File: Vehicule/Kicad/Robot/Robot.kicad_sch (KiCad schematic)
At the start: 3 parts, among them U1 ESP32-C3_SUPERMINI, U2 L293D, U3 Regulator-DFR0569

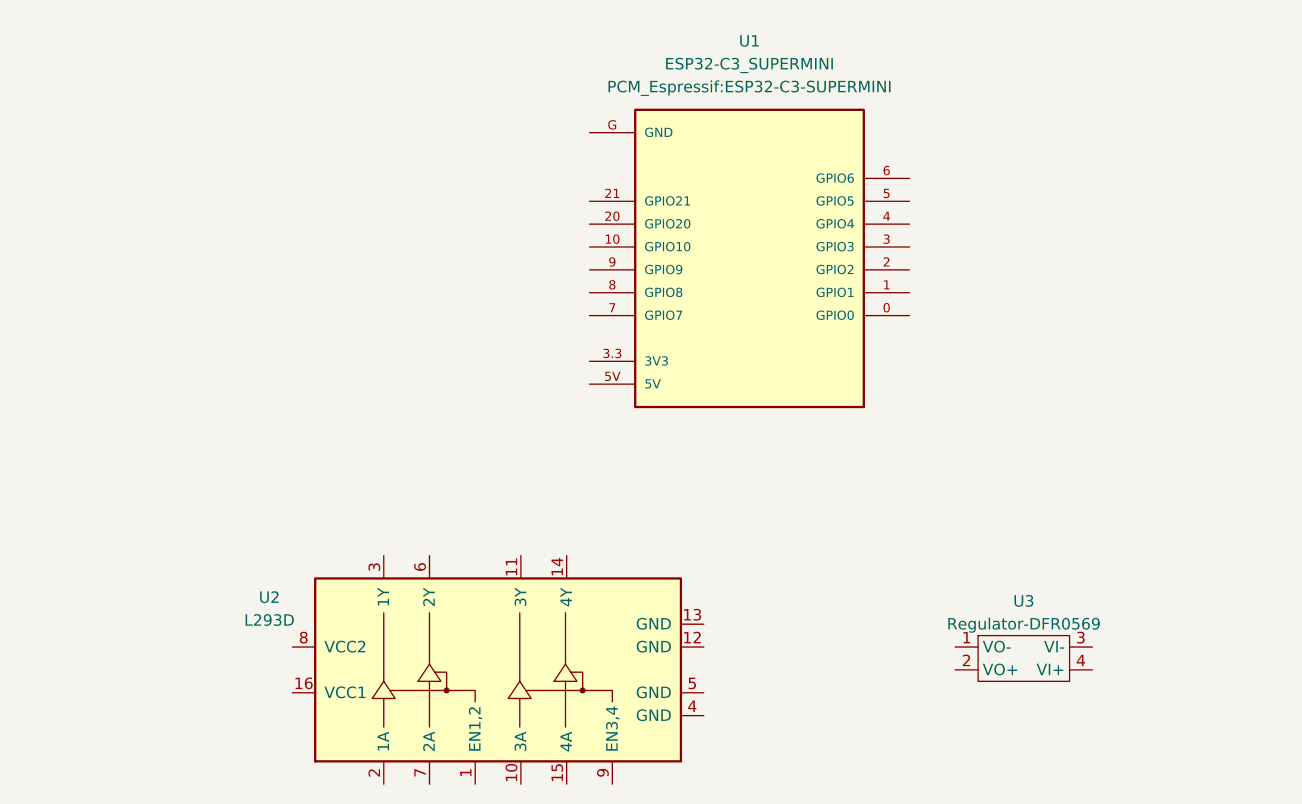
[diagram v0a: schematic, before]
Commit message: Schema et implantation du circuit pour le robot
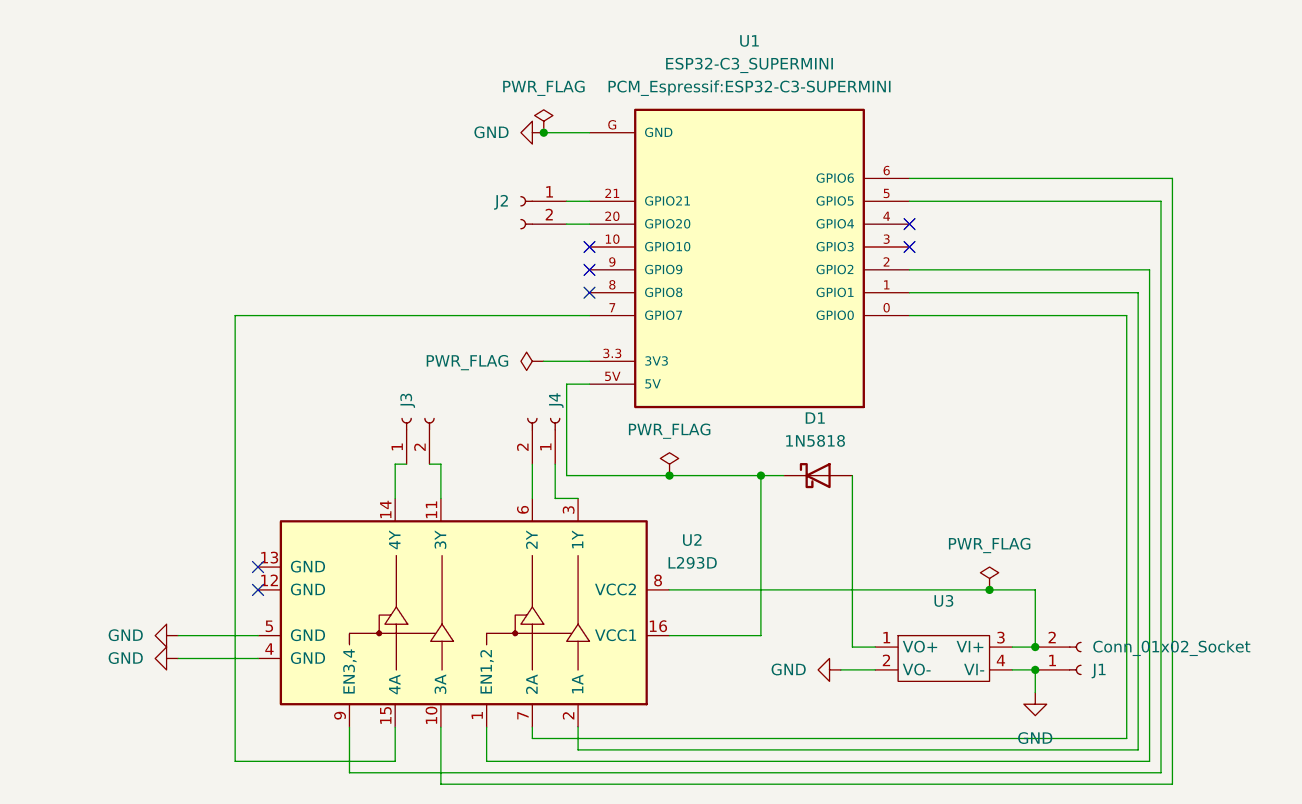
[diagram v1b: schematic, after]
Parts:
- added D1: 1N5818, Diode_THT:D_DO-41_SOD81_P10.16mm_Horizontal, symbol Diode:1N5818
- added J1, J2, J3, J4: Conn_01x02_Socket, Empreintes:CONN-2-PINS, symbol Connector:Conn_01x02_Socket
- U3: value Regulator-DFR0569 -> ~
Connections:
- net at U2.1 (EN1,2): now also U1.2 (GPIO2)
- net at U2.10 (3A): now also U1.6 (GPIO6)
- net at U2.11 (3Y): now also J3.2 (Pin_2)
- net at U2.14 (4Y): now also J3.1 (Pin_1)
- net at U2.15 (4A): now also U1.7 (GPIO7)
- net at U2.16 (VCC1): now also U1.5V, D1.1 (K)
- net at U2.2 (1A): now also U1.1 (GPIO1)
- net at U2.3 (1Y): now also J4.1 (Pin_1)
- net GND: now reaches U2.4 (GND)
- net GND: now also U1.G (GND), U2.5 (GND), U3.2 (VO-), U3.4 (VI-), J1.1 (Pin_1)
- net at U2.6 (2Y): now also J4.2 (Pin_2)
- net at U2.7 (2A): now also U1.0 (GPIO0)
- net at U2.8 (VCC2): now also U3.3 (VI+), J1.2 (Pin_2)
- net at U2.9 (EN3,4): now also U1.5 (GPIO5)
- net at U1.20 (GPIO20): now also J2.2 (Pin_2)
- net at U1.21 (GPIO21): now also J2.1 (Pin_1)
- net at U3.1 (VO+): now also D1.2 (A)
- no-connect marks 0 -> 7
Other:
- moved on the sheet: U2

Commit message: Transfert du SUPERMINI (composant et empreintes) dans les librairies locales (Anumby et Empreintes) Renommer Empreintes -> Anumby
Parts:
- J1, J2, J3, J4: footprint Empreintes:CONN-2-PINS -> Anumby:CONN-2-PINS
- U1: footprint PCM_Espressif:ESP32-C3-SUPERMINI -> Anumby:ESP32-C3-SUPERMINI
- U3: footprint Empreintes:Regulator-DFR0569 -> Anumby:Regulator-DFR0569
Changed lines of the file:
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@@
 			)
 		)
-		(property "Footprint" "Empreintes:CONN-2-PINS"
+		(property "Footprint" "Anumby:CONN-2-PINS"
 			(at 80.01 86.36 0)
 			(effects
@@
 			)
 		)
-		(property "Footprint" "PCM_Espressif:ESP32-C3-SUPERMINI"
+		(property "Footprint" "Anumby:ESP32-C3-SUPERMINI"
 			(at 101.6 49.53 0)
 			(effects
@@
 			)
 		)
-		(property "Footprint" "Empreintes:CONN-2-PINS"
+		(property "Footprint" "Anumby:CONN-2-PINS"
 			(at 63.5 86.36 0)
 			(effects
@@
 			)
 		)
-		(property "Footprint" "Empreintes:CONN-2-PINS"
+		(property "Footprint" "Anumby:CONN-2-PINS"
 			(at 138.43 114.3 0)
 			(effects
@@
 			)
 		)
-		(property "Footprint" "Empreintes:CONN-2-PINS"
+		(property "Footprint" "Anumby:CONN-2-PINS"
 			(at 76.2 62.23 0)
 			(effects
@@
 			)
 		)
-		(property "Footprint" "Empreintes:Regulator-DFR0569"
+		(property "Footprint" "Anumby:Regulator-DFR0569"
 			(at 121.92 111.76 0)
 			(effects

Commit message: Ajout de la couche de masse pour Robot Ajout d'un connecteur 1 pin Mise à jour de tous les PCB et les Schémas
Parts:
- removed J1, J2, J3, J4: Conn_01x02_Socket, Anumby:CONN-2-PINS, symbol Connector:Conn_01x02_Socket
- added J1, J2: Conn_01x02_Socket, Anumby:CONN-2-PINS, symbol Anumby:Conn_01x02_Socket
- added J3, J4, J5, J6: Conn_01x01_Socket, Anumby:CONN-1-PINS, symbol Anumby:Conn_01x01_Socket
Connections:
- net GND: now also J1.2 (Pin_2)
- net at U2.3 (1Y): now also J6.1 (Pin_1)
- net at U2.6 (2Y): now also J5.1 (Pin_1)
- net at U2.11 (3Y): now also J4.1 (Pin_1)
- net at U2.14 (4Y): now also J3.1 (Pin_1)
- net at U2.8 (VCC2), U3.3 (VI+): now also J1.1 (Pin_1)
- net at U1.20 (GPIO20): now also J2.2 (Pin_2)
- net at U1.21 (GPIO21): now also J2.1 (Pin_1)

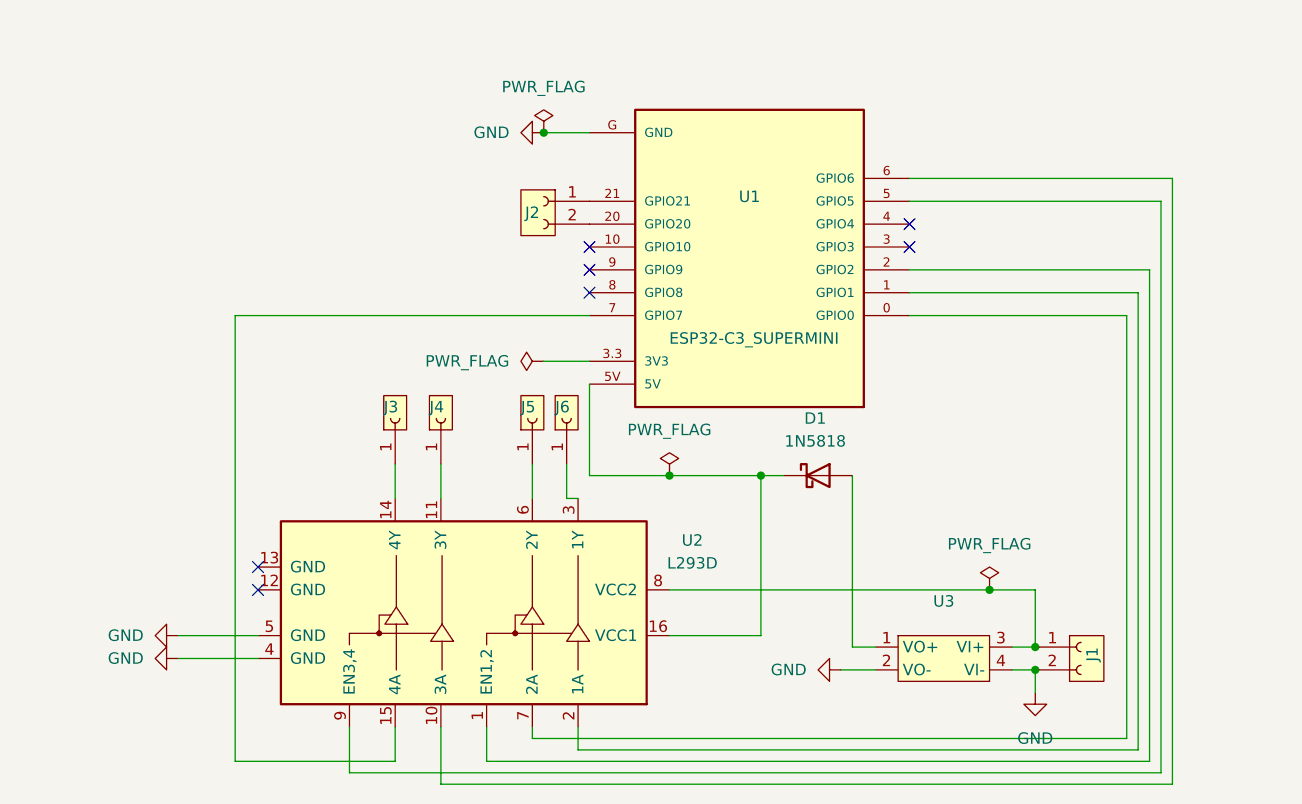
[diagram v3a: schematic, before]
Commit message: Ajout de logo Anumby pour PCB Mise à jour des empreintes, des connecteurs des librairies
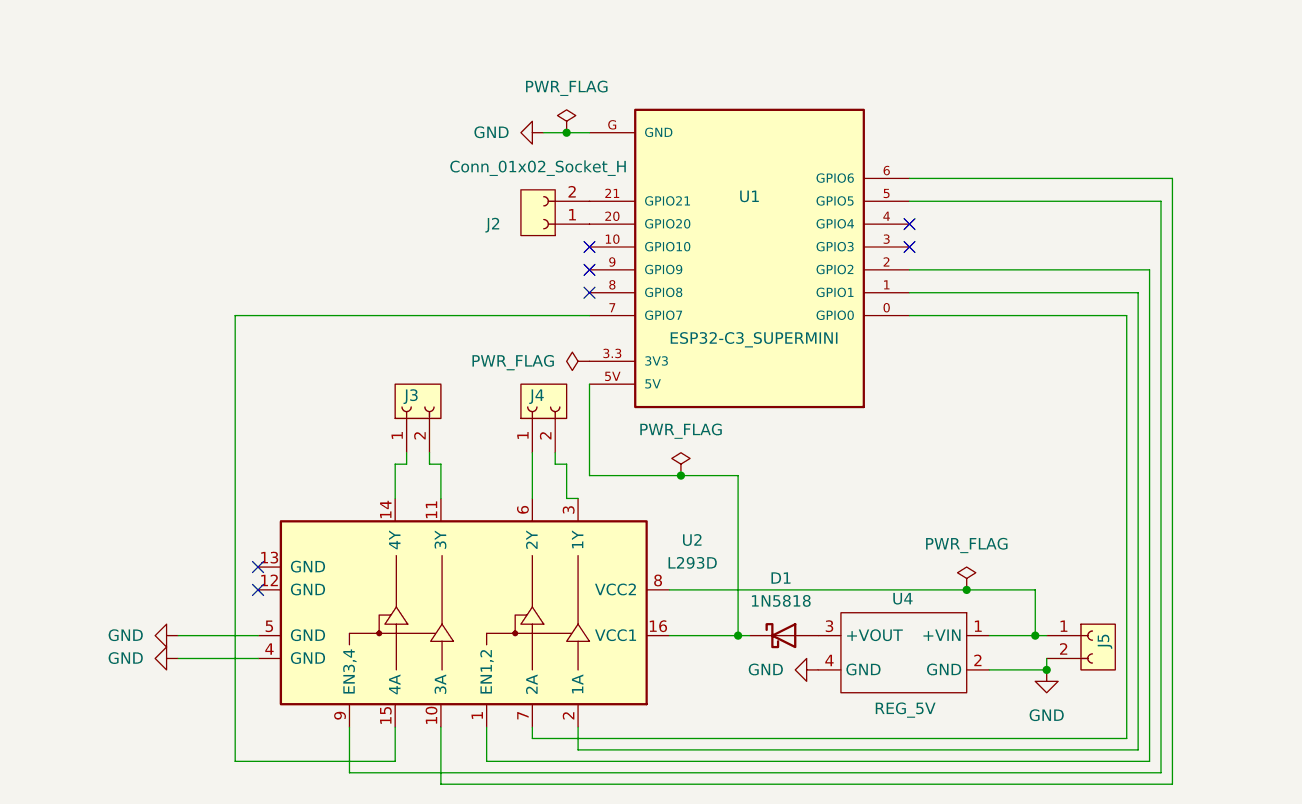
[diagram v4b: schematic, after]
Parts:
- removed J1, J2: Conn_01x02_Socket, Anumby:CONN-2-PINS, symbol Anumby:Conn_01x02_Socket
- removed J3, J4, J5, J6: Conn_01x01_Socket, Anumby:CONN-1-PINS, symbol Anumby:Conn_01x01_Socket
- removed U3: ~, Anumby:Regulator-DFR0569, symbol Anumby:Regulator-DFR0569
- added J2, J3, J4, J5: Conn_01x02_Socket_H, Connector_JST:JST_EH_B2B-EH-A_1x02_P2.50mm_Vertical, symbol Anumby:Conn_01x02_Socket_V
- added U4: REG_5V, Anumby:REG_5V_DFR, symbol Gilles_Library:REG_5V_DFR
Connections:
- net GND: now also J5.2 (Pin_2), U4.2 (GND), U4.4 (GND)
- net at U2.11 (3Y): now also J3.2 (Pin_2)
- net at U2.14 (4Y): now also J3.1 (Pin_1)
- net at U2.3 (1Y): now also J4.2 (Pin_2)
- net at U2.6 (2Y): now also J4.1 (Pin_1)
- net at U2.8 (VCC2): now also J5.1 (Pin_1), U4.1 (+VIN)
- net at U1.20 (GPIO20): now also J2.1 (Pin_1)
- net at U1.21 (GPIO21): now also J2.2 (Pin_2)
- net at D1.2 (A): now also U4.3 (+VOUT)
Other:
- moved on the sheet: D1

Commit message: Finalisation du PCB du Robot puis génération des fichiers de fabrication Gerber
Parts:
- added SW1: SW_DPDT_x2, Button_Switch_THT:SW_Slide_SPDT_Straight_CK_OS102011MS2Q, symbol Gilles_Library:SW_DPDT_x2
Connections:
- net at J5.1 (Pin_1), U4.1 (+VIN): now also SW1.1 (A); no longer U2.8 (VCC2)
- new net: SW1.2 (B), U2.8 (VCC2)
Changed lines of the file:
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@@
+	)
+	(junction
+		(at 124.46 99.06)
+		(diameter 0)
+		(color 0 0 0 0)
 	)
 	(junction
@@
 	)
 	(junction
-		(at 125.73 105.41)
-		(diameter 0)
-		(color 0 0 0 0)
-	)
-	(junction
 		(at 81.28 54.61)
 		(diameter 0)
@@
 	(wire
 		(pts
-			(xy 92.71 105.41) (xy 125.73 105.41)
-		)
-		(stroke
-			(width 0)
-			(type default)
-		)
-	)
-	(wire
-		(pts
 			(xy 77.47 120.65) (xy 77.47 121.92)
 		)
@@
 	(wire
 		(pts
-			(xy 125.73 105.41) (xy 133.35 105.41)
+			(xy 92.71 101.6) (xy 92.71 105.41)
+		)
+		(stroke
+			(width 0)
+			(type default)
+		)
+	)
+	(wire
+		(pts
+			(xy 124.46 99.06) (xy 133.35 99.06)
 		)
 		(stroke
@@
 	(wire
 		(pts
+			(xy 118.11 99.06) (xy 124.46 99.06)
+		)
+		(stroke
+			(width 0)
+			(type default)
+		)
+	)
+	(wire
+		(pts
 			(xy 80.01 90.17) (xy 80.01 91.44)
 		)
@@
 	(wire
 		(pts
-			(xy 133.35 105.41) (xy 133.35 110.49)
+			(xy 133.35 99.06) (xy 133.35 110.49)
 		)
 		(stroke
@@
 		(pts
 			(xy 134.62 114.3) (xy 134.62 113.03)
+		)
+		(stroke
+			(width 0)
+			(type default)
+		)
+	)
+	(wire
+		(pts
+			(xy 107.95 101.6) (xy 92.71 101.6)
 		)
 		(stroke
@@
 		(dnp no)
 		(property "Reference" "U2"
-			(at 95.25 99.9138 90)
+			(at 72.39 104.902 90)
 			(effects
 				(font
@@
 		)
 		(property "Value" "L293D"
-			(at 95.25 102.4538 90)
+			(at 72.39 106.934 90)
 			(effects
 				(font
@@
 	(symbol
 		(lib_id "power:PWR_FLAG")
-		(at 125.73 105.41 0)
+		(at 124.46 99.06 0)
 		(unit 1)
 		(exclude_from_sim no)
@@
 		(fields_autoplaced yes)
 		(property "Reference" "#FLG01"
-			(at 125.73 103.505 0)
+			(at 124.46 97.155 0)
 			(effects
 				(font
@@
 		)
 		(property "Value" "PWR_FLAG"
-			(at 125.73 100.33 0)
+			(at 124.46 93.98 0)
 			(effects
 				(font
@@
 		)
 		(property "Footprint" ""
-			(at 125.73 105.41 0)
+			(at 124.46 99.06 0)
 			(effects
 				(font
@@
 		)
 		(property "Datasheet" "~"
-			(at 125.73 105.41 0)
+			(at 124.46 99.06 0)
 			(effects
 				(font
@@
 		)
 		(property "Description" "Special symbol for telling ERC where power comes from"
-			(at 125.73 105.41 0)
+			(at 124.46 99.06 0)
 			(effects
 				(font
@@
 					(unit 1)
 				)
+			)
+		)
+	)
+	(symbol
+		(lib_id "Gilles_Library:SW_DPDT_x2")
+		(at 113.03 101.6 0)
+		(unit 1)
+		(exclude_from_sim no)
+		(in_bom yes)
+		(on_board yes)
+		(dnp no)
+		(fields_autoplaced yes)
+		(property "Reference" "SW1"
+			(at 113.03 92.71 0)
+			(effects
+				(font
+					(size 1.27 1.27)
+				)
+			)
+		)
+		(property "Value" "SW_DPDT_x2"
+			(at 113.03 95.25 0)
+			(effects
+				(font
+					(size 1.27 1.27)
+				)
+			)
+		)
+		(property "Footprint" "Button_Switch_THT:SW_Slide_SPDT_Straight_CK_OS102011MS2Q"
+			(at 113.03 101.6 0)
+			(effects
+				(font
+					(size 1.27 1.27)
+				)
+				(hide yes)
+			)
+		)
+		(property "Datasheet" "~"
+			(at 113.03 101.6 0)
+			(effects
+				(font
+					(size 1.27 1.27)
+				)
+				(hide yes)
+			)
+		)
+		(property "Description" "Switch, dual pole double throw, separate symbols"
+			(at 113.03 101.6 0)
+			(effects
+				(font
+					(size 1.27 1.27)
+				)
+				(hide yes)
+			)
+		)
+		(pin "5"
+		)
+		(pin "1"
+		)
+		(pin "6"
+		)
+		(pin "2"
+		)
+		(pin "4"
+		)
+		(pin "3"
+		)
+		(instances
+			(project ""
+				(path "/27edc304-32a2-4dcd-b20b-7abf96794b2d"
+					(reference "SW1")
+					(unit 1)
+				)

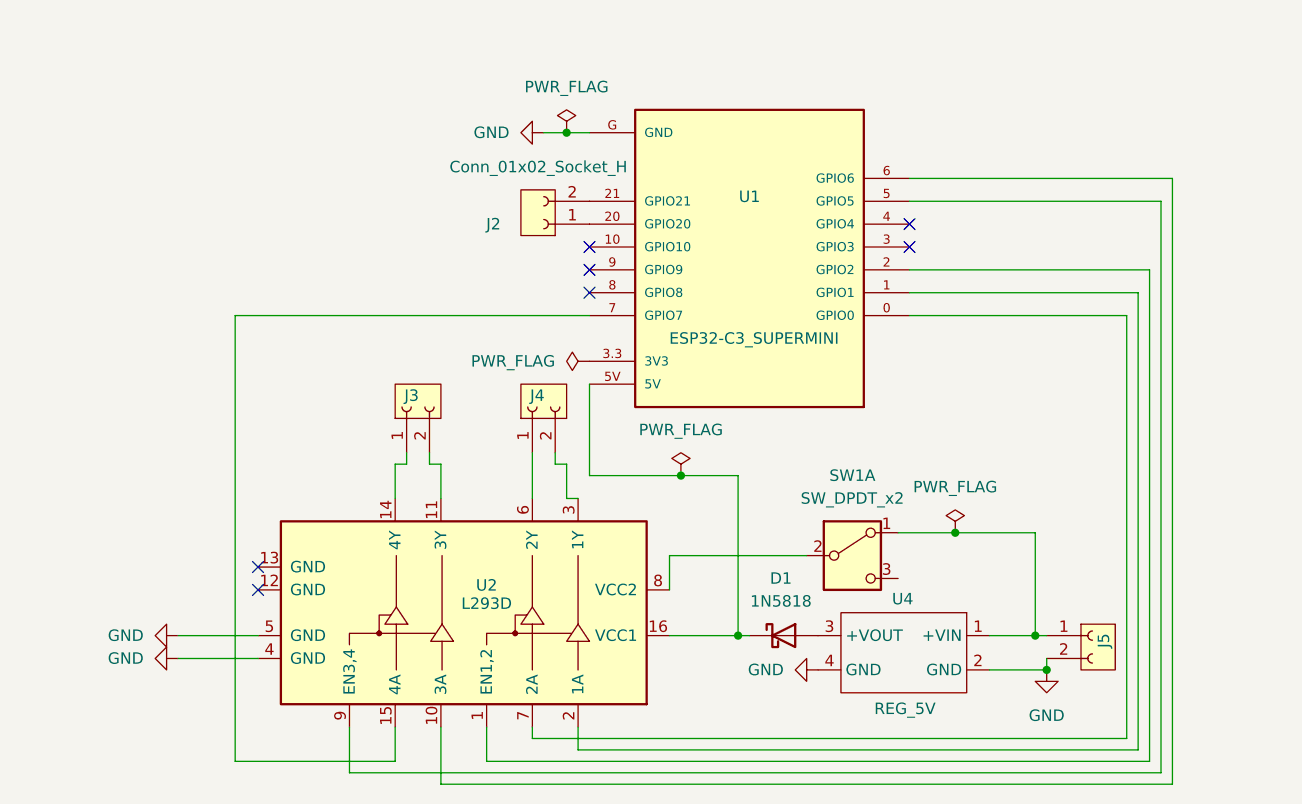
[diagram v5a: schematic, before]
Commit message: Remplacement de l'empreinte ESP32 de surface pour une empreinte traversante
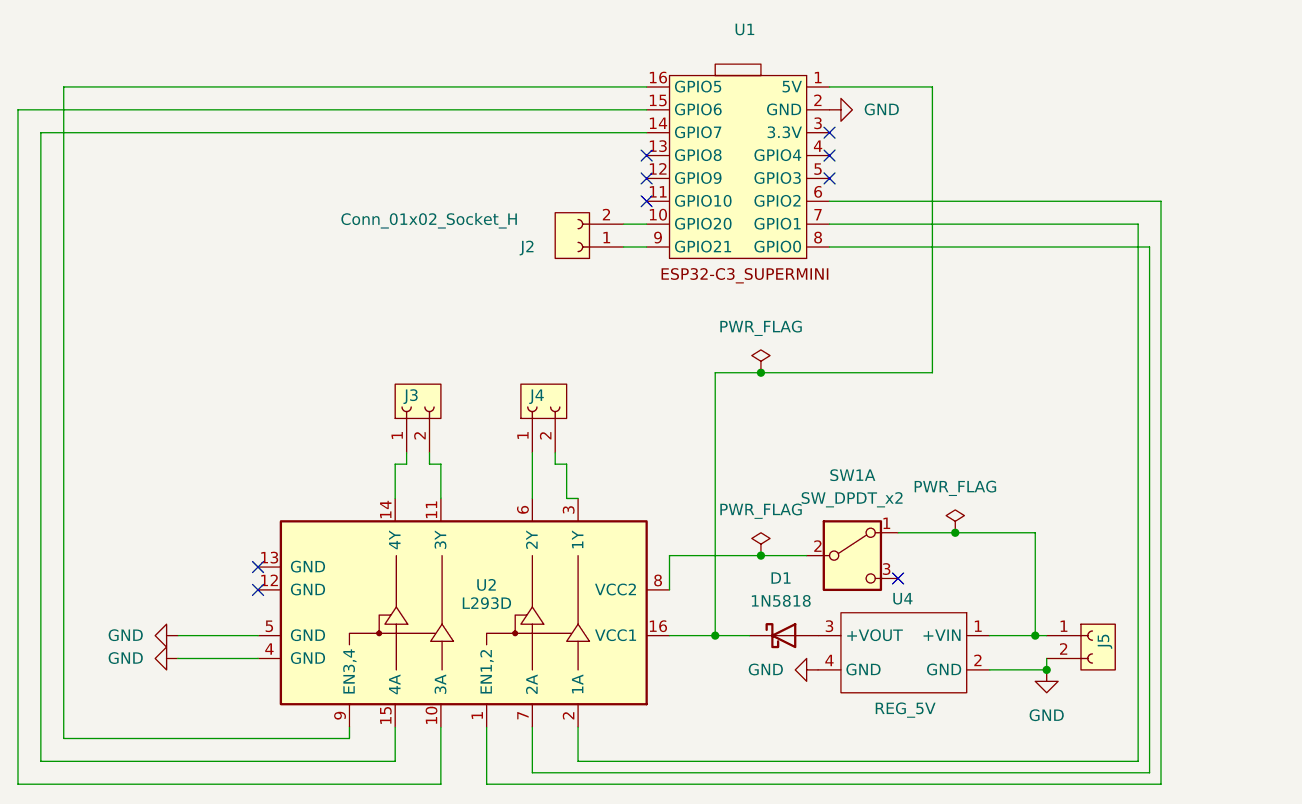
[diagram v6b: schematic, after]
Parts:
- removed U1: ESP32-C3_SUPERMINI, Anumby:ESP32-C3-SUPERMINI, symbol PCM_ESP32-C3-SUPERMINI:ESP32-C3_SUPERMINI
- added U1: ~, Anumby:ESP32-C3_SUPERMINI, symbol Gilles_Library:ESP32-C3_MINI
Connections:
- net GND: now also U1.2 (GND)
- net at U2.1 (EN1,2): now also U1.6 (GPIO2)
- net at U2.10 (3A): now also U1.15 (GPIO6)
- net at U2.15 (4A): now also U1.14 (GPIO7)
- net at D1.1 (K), U2.16 (VCC1): now also U1.1 (5V)
- net at U2.2 (1A): now also U1.7 (GPIO1)
- net at U2.7 (2A): now also U1.8 (GPIO0)
- net at U2.9 (EN3,4): now also U1.16 (GPIO5)
- net at J2.1 (Pin_1): now also U1.9 (GPIO21)
- net at J2.2 (Pin_2): now also U1.10 (GPIO20)
- no-connect marks 7 -> 9
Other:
- moved on the sheet: J2
